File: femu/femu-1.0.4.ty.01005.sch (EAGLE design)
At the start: 56 parts, among them IC1 ESP32-QFN_5X5

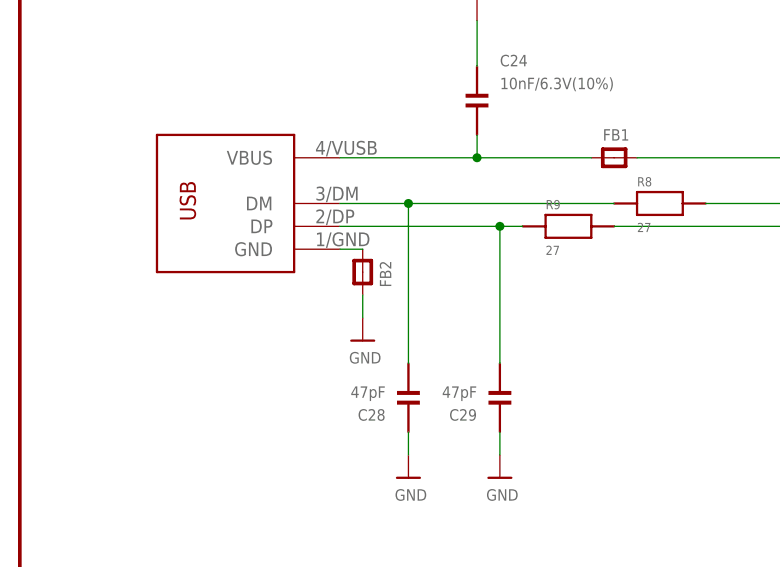
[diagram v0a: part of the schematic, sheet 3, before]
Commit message: Adjusting antenna and ground plane in femu-1.0.4.ty.01005 design. 11.35mil wide RF trace, 5mil isolation. At PCBWay 0.8mm thick PCB (0.175mm thick dialectric, constant 4.29)(copper thickness of 18um) ...should yield 50ohm impedance at 2448MHz (2.4GHz)
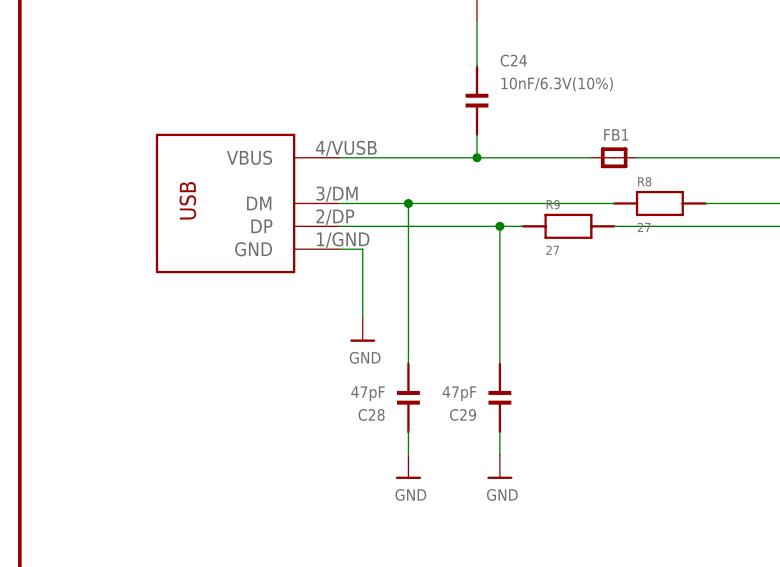
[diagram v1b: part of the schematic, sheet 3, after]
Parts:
- removed FB2: (no value), microbuilder:FERRITE_0402MP
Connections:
- removed net N$11: FB2.P$1, U$37.GND
- net GND: now also U$37.GND; no longer FB2.P$2
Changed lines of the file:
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@@
 <attribute name="SPICEPREFIX" value="U"/>
-</part>
-<part name="FB2" library="microbuilder" deviceset="FERRITE" device="_0402MP">
-<attribute name="MPN" value="BLM15PD121SN1D"/>
-<attribute name="SPICEPREFIX" value="F"/>
 </part>
 <part name="U$3" library="microbuilder" deviceset="GND" device=""/>
@@
 <attribute name="VALUE" x="140.716" y="106.68" size="1.27" layer="96"/>
 </instance>
-<instance part="FB2" gate="G$1" x="38.1" y="55.88" smashed="yes" rot="R270">
-<attribute name="NAME" x="40.005" y="57.15" size="1.27" layer="95" rot="R270"/>
-<attribute name="VALUE" x="34.925" y="57.15" size="1.27" layer="95" rot="R270"/>
-<attribute name="MPN" x="38.1" y="55.88" size="1.778" layer="96" rot="R270" display="off"/>
-</instance>
 </instances>
 <busses>
@@
 <segment>
 <pinref part="U$44" gate="G$1" pin="GND"/>
-<pinref part="FB2" gate="G$1" pin="P$2"/>
-<wire x1="38.1" y1="50.8" x2="38.1" y2="53.34" width="0.1524" layer="91"/>
+<pinref part="U$37" gate="A" pin="GND"/>
+<wire x1="38.1" y1="58.42" x2="35.56" y2="58.42" width="0.1524" layer="91"/>
+<wire x1="38.1" y1="50.8" x2="38.1" y2="58.42" width="0.1524" layer="91"/>
 </segment>
 <segment>
@@
 </segment>
 </net>
-<net name="N$11" class="0">
-<segment>
-<pinref part="U$37" gate="A" pin="GND"/>
-<pinref part="FB2" gate="G$1" pin="P$1"/>
-<wire x1="38.1" y1="58.42" x2="35.56" y2="58.42" width="0.1524" layer="91"/>
-</segment>
-</net>

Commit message: Adjusting ground pours.
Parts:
- U$6: value FEMU-EDGE-CONNECTOR -> FEMU-EDGE-CONNECTORFEMU-EDGE-CONN-SLIM; device femu-edge-connectors:FEMU-EDGE-CONNECTOR -> femu-edge-connectors:FEMU-EDGE-CONNECTORFEMU-EDGE-CONN-SLIM
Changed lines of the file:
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@@
 <part name="U$36" library="microbuilder" deviceset="VIN" device=""/>
 <part name="U$46" library="microbuilder" deviceset="GND" device=""/>
-<part name="U$6" library="femu-edge-connectors" deviceset="FEMU-EDGE-CONNECTOR" device=""/>
+<part name="U$6" library="femu-edge-connectors" deviceset="FEMU-EDGE-CONNECTOR" device="FEMU-EDGE-CONN-SLIM" value="FEMU-EDGE-CONNECTORFEMU-EDGE-CONN-SLIM"/>
 <part name="U$17" library="microbuilder" deviceset="GND" device=""/>
 <part name="U$18" library="microbuilder" deviceset="3.3V" device=""/>

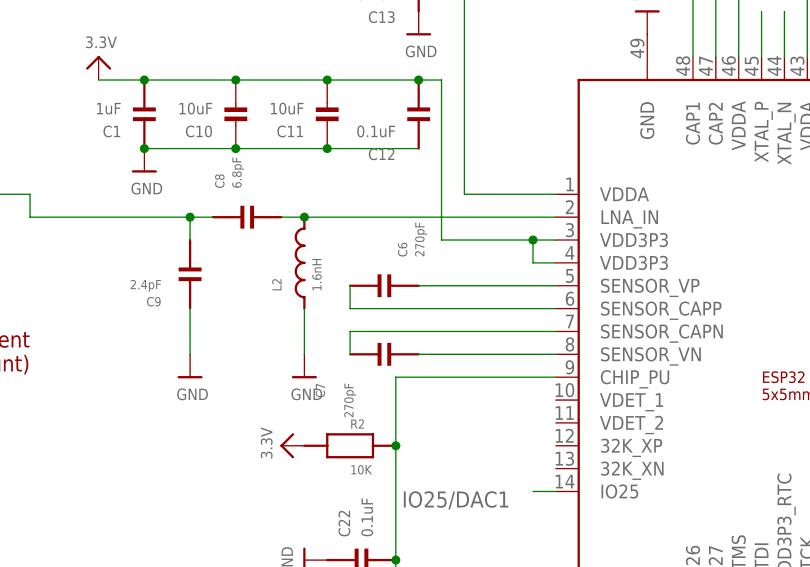
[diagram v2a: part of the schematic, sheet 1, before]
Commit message: Adjusted trace width and distance for 35ohm impedance
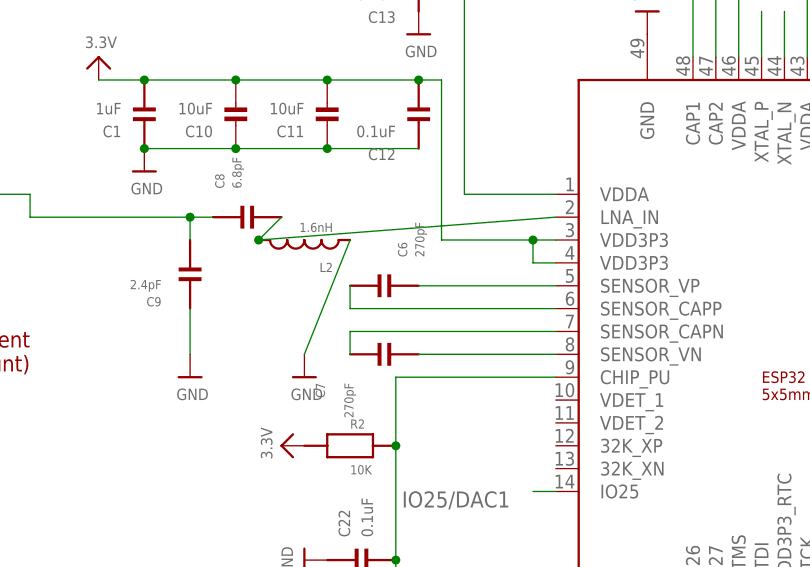
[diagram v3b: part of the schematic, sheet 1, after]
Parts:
- U$38: MPN (none) -> AH212M245001-T
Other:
- moved on the sheet: L2
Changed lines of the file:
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@@
 </part>
 <part name="U$5" library="microbuilder" deviceset="GND" device=""/>
-<part name="U$38" library="taydo-yuden-rf-antenna" deviceset="AF216M245001-T" device=""/>
+<part name="U$38" library="taydo-yuden-rf-antenna" deviceset="AF216M245001-T" device="">
+<attribute name="MPN" value="AH212M245001-T"/>
+</part>
 </parts>
 <sheets>
@@
 <attribute name="MPN" x="81.28" y="129.54" size="1.778" layer="96" rot="R90" display="off"/>
 </instance>
-<instance part="L2" gate="G$1" x="86.36" y="124.46" smashed="yes" rot="R90">
-<attribute name="NAME" x="83.82" y="121.285" size="1.016" layer="95" font="vector" rot="R90"/>
-<attribute name="VALUE" x="88.265" y="121.285" size="1.016" layer="96" font="vector" rot="R90"/>
-<attribute name="MPN" x="86.36" y="124.46" size="1.778" layer="96" rot="R90" display="off"/>
+<instance part="L2" gate="G$1" x="86.36" y="127" smashed="yes" rot="R180">
+<attribute name="NAME" x="89.535" y="124.46" size="1.016" layer="95" font="vector" rot="R180"/>
+<attribute name="VALUE" x="89.535" y="128.905" size="1.016" layer="96" font="vector" rot="R180"/>
+<attribute name="MPN" x="86.36" y="127" size="1.778" layer="96" rot="R180" display="off"/>
 </instance>
 <instance part="C9" gate="G$1" x="73.66" y="124.46" smashed="yes" rot="R180">
@@
 <pinref part="L2" gate="G$1" pin="P$1"/>
 <pinref part="U$3" gate="G$1" pin="GND"/>
-<wire x1="86.36" y1="119.38" x2="86.36" y2="114.3" width="0.1524" layer="91"/>
+<wire x1="91.44" y1="127" x2="86.36" y2="114.3" width="0.1524" layer="91"/>
 </segment>
 </net>
@@
 <segment>
 <pinref part="IC1" gate="G$1" pin="LNA_IN"/>
-<wire x1="114.3" y1="129.54" x2="86.36" y2="129.54" width="0.1524" layer="91"/>
+<wire x1="114.3" y1="129.54" x2="81.28" y2="127" width="0.1524" layer="91"/>
 <pinref part="L2" gate="G$1" pin="P$2"/>
 <pinref part="C8" gate="G$1" pin="P$2"/>
-<wire x1="83.82" y1="129.54" x2="86.36" y2="129.54" width="0.1524" layer="91"/>
-<junction x="86.36" y="129.54"/>
-</segment>
-</net>
+<wire x1="83.82" y1="129.54" x2="81.28" y2="127" width="0.1524" layer="91"/>
+<junction x="81.28" y="127"/>
+</segment>
+</net>
